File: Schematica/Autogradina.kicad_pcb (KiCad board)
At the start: 2 copper layers, 50 parts, among them J1 Power_Connector, J2 AC_Connector, J3 UART_Connector, J4 USB_B_Micro, J5 Boot_Jumper, J6 Ports_Connector, J7 Conn_01x02_Socket, J8 Conn_01x02_Socket, J9 Conn_01x02_Socket, Q1 IRLZ44N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

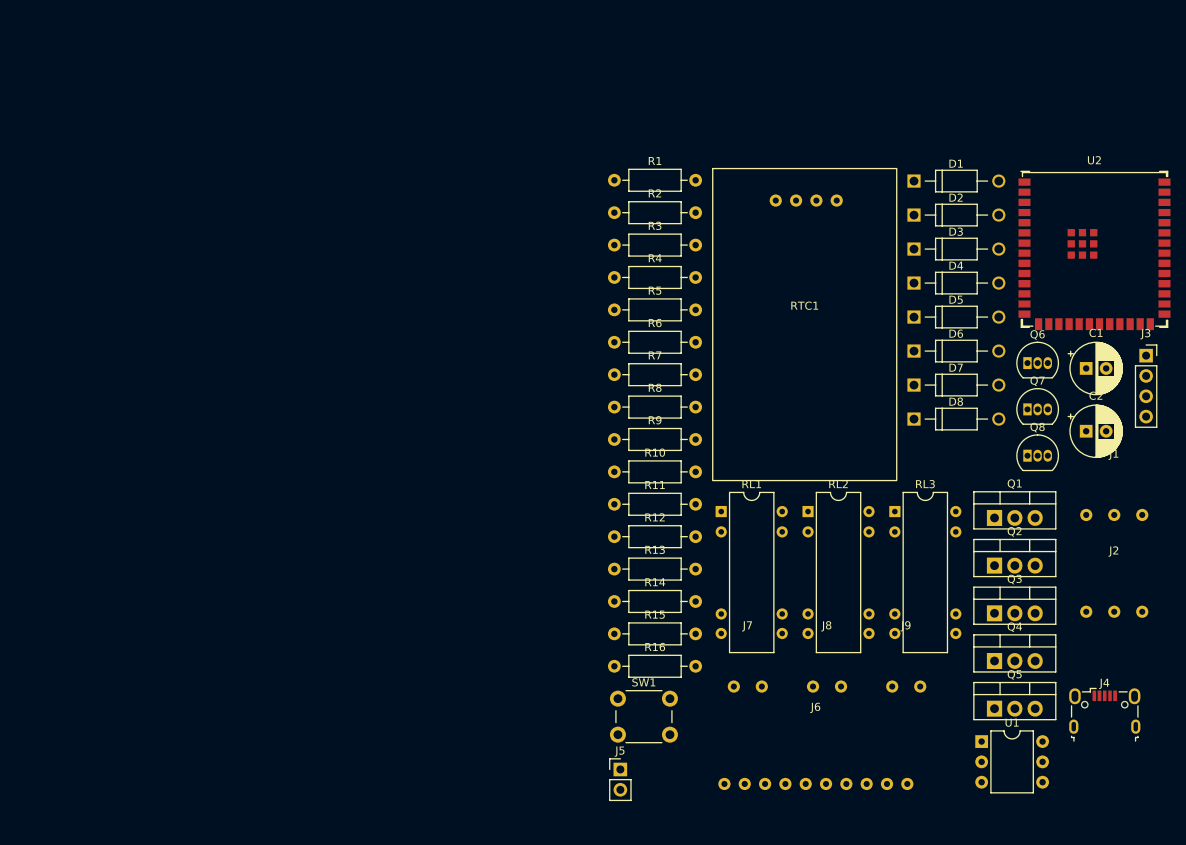
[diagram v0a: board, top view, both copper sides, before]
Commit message: Updated schematic, board; Almost finished board
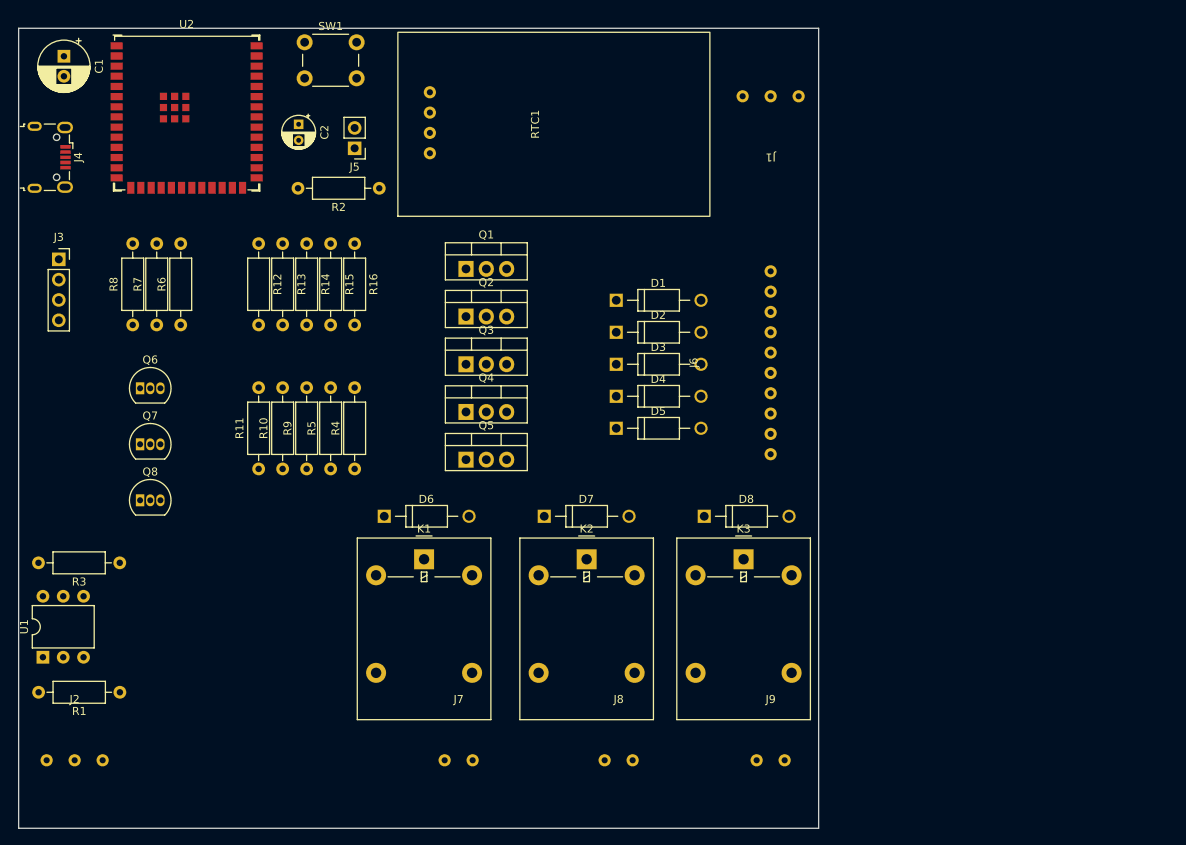
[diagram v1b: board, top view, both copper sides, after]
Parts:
- removed RL1, RL2, RL3: DIPxx-1Axx-11x, Relay_THT:Relay_StandexMeder_DIP_LowProfile
- added K1: G5LE-1, Relay_THT:Relay_SPDT_Omron-G5LE-1, F.Cu at (78.7, 93.4)
- added K2: G5LE-1, Relay_THT:Relay_SPDT_Omron-G5LE-1, F.Cu at (99.0, 93.4)
- added K3: G5LE-1, Relay_THT:Relay_SPDT_Omron-G5LE-1, F.Cu at (118.6, 93.4)
- C2: footprint Capacitor_THT:CP_Radial_D6.3mm_P2.50mm -> Capacitor_THT:CP_Radial_D4.0mm_P2.00mm
- R6, R7, R8: value 10k -> 5k
- moved J4 148.9 mm to (31.9, 43.1), turned to -90 degrees
- moved J3 136.4 mm to (33.0, 55.9)
- moved C1 133.6 mm to (33.7, 30.5), turned to -90 degrees
- moved J2 131.3 mm to (35.0, 118.5)
- moved U1 117.8 mm to (31.0, 105.6), turned to 90 degrees
- moved U2 114.8 mm to (49.0, 37.5)
- moved Q8 111.1 mm to (43.2, 86.0)
- moved Q7 111.0 mm to (43.2, 79.0)
- moved Q6 111.0 mm to (43.2, 72.0)
- moved C2 105.7 mm to (63.0, 39.0), turned to -90 degrees
- moved SW1 90.9 mm to (63.8, 28.8)
- moved R1 89.0 mm to (40.7, 110.0), turned to 180 degrees
- moved J5 84.5 mm to (70.0, 42.0), turned to 180 degrees
- moved R3 73.5 mm to (40.6, 93.8), turned to 180 degrees
- moved Q2 73.0 mm to (83.9, 63.0)
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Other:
- board outline added: 100 x 100 mm
- rule pad_to_mask_clearance: 0 -> 0.05

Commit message: Routing changes
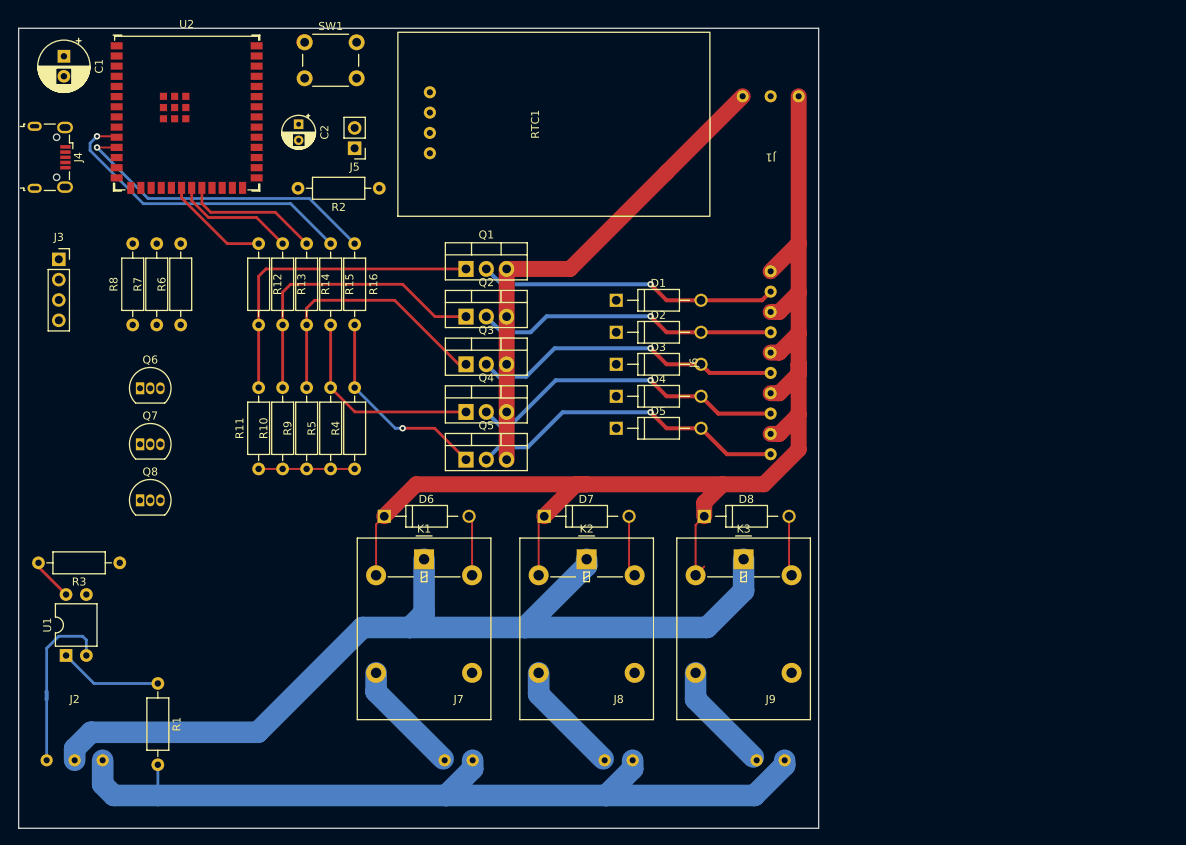
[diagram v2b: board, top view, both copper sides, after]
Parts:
- added NT2: NetTie_2, NetTie:NetTie-2_SMD_Pad0.5mm, B.Cu at (31.5, 110.4)
- U1: value 4N25 -> PC817; footprint Package_DIP:DIP-6_W7.62mm -> Package_DIP:DIP-4_W7.62mm
- moved R1 4.87 mm to (45.4, 108.9), turned to -90 degrees
- moved U1 2.90 mm to (33.9, 105.4)
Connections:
- U1 pad 2: AC_G -> Net-(NT2-Pad2)
- U1 pad 3: unconnected-(U1-NC-Pad3) -> GND
- U1 pad 4: GND -> N_To_Ground_Probe
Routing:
- net 12V: track 0.00 -> 161.3 mm
- net AC_L: track 0.00 -> 118.2 mm
- net AC_N: track 0.00 -> 106.4 mm
- net GND: track 0.00 -> 74.3 mm
- net Net-(D4-A): track 0.00 -> 40.6 mm, vias 0 -> 1
- net Net-(Q1-G): track 0.00 -> 40.2 mm
- net Net-(D5-A): track 0.00 -> 40.2 mm, vias 0 -> 1
- net Mosfet_Port5: track 0.00 -> 39.6 mm, vias 0 -> 1
- net Mosfet_Port4: track 0.00 -> 39.5 mm, vias 0 -> 1
- net Net-(D3-A): track 0.00 -> 38.9 mm, vias 0 -> 1
- net Net-(D2-A): track 0.00 -> 38.0 mm, vias 0 -> 1
- net Net-(D1-A): track 0.00 -> 37.6 mm, vias 0 -> 1
- net Net-(Q2-G): track 0.00 -> 36.9 mm
- net Net-(Q3-G): track 0.00 -> 33.6 mm
- net Net-(Q4-G): track 0.00 -> 26.0 mm
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
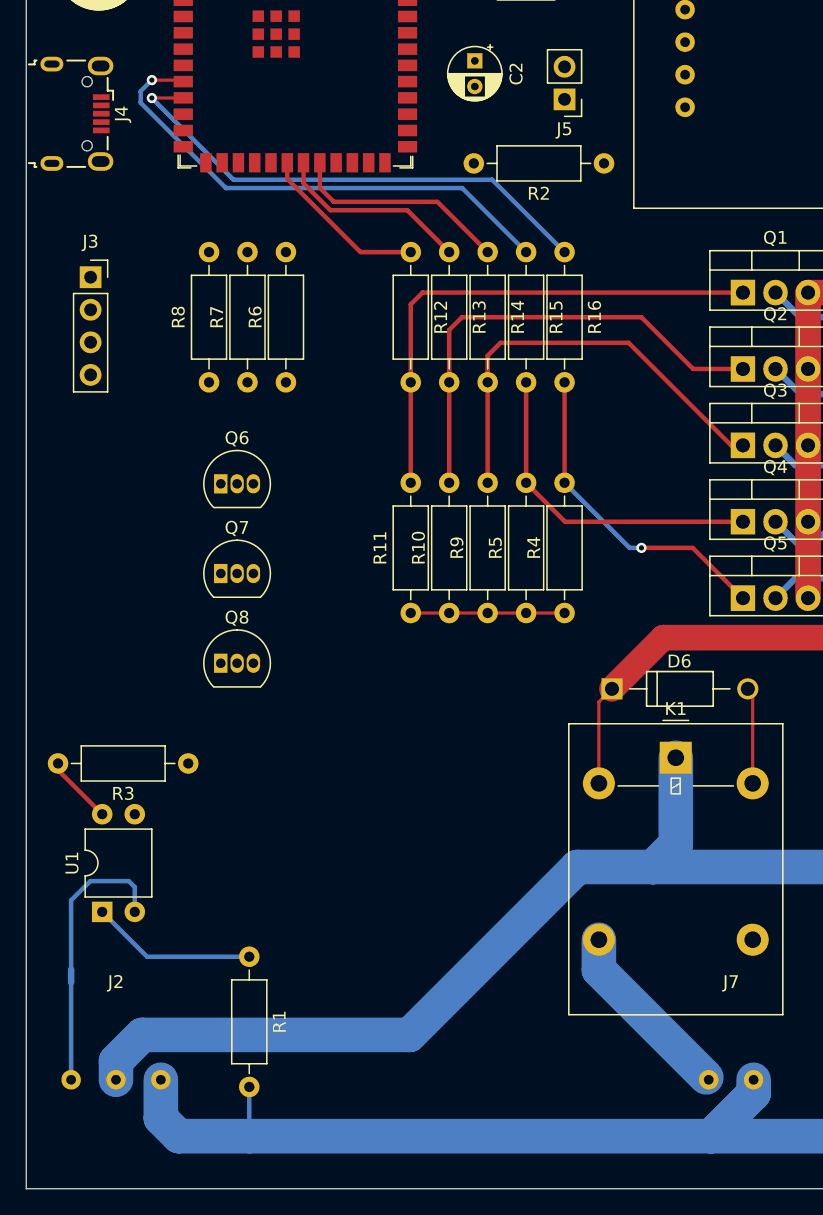
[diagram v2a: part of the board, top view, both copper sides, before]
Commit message: Repaired too small tracks
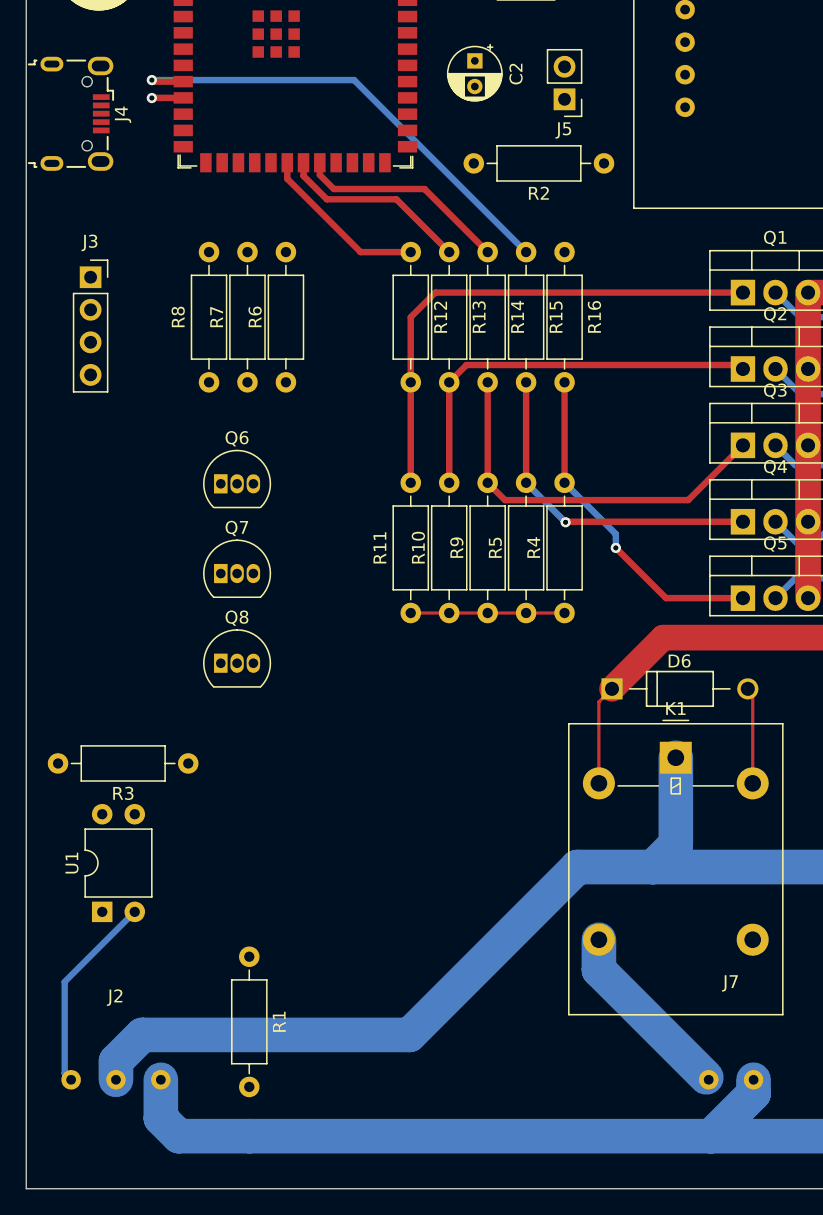
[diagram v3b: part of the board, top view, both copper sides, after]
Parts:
- removed NT2: NetTie_2, NetTie:NetTie-2_SMD_Pad0.5mm
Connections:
- U1 pad 2: Net-(NT2-Pad2) -> AC_G
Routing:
- net Mosfet_Port5: track 39.6 -> 2.47 mm
- net Net-(NT2-Pad2): track 13.0 -> 0.00 mm
- net Net-(R1-Pad1): track 12.9 -> 0.00 mm
- net AC_G: track 7.55 -> 15.6 mm
- net Net-(Q2-G): track 36.9 -> 31.4 mm
- net N_To_Ground_Probe: track 5.39 -> 0.00 mm
- net AC_N: track 106.4 -> 102.6 mm
- net Net-(Q3-G): track 33.6 -> 30.1 mm
- net Mosfet_Port4: track 39.5 -> 37.4 mm
- net Net-(Q5-G): track 25.5 -> 26.1 mm
- net Mosfet_Port3: track 17.7 -> 17.1 mm
- net Net-(Q1-G): track 40.2 -> 39.6 mm
- net Net-(Q4-G): track 26.0 -> 26.1 mm, vias 0 -> 1
